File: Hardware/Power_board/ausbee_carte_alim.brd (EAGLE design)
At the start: 64.8 x 71.4 mm, 21 parts

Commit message: modification on power board: add relay and fuse
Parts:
- added D1: 1N4148DO35-10, diode:DO35-10
- added JP1: (no value), pinhead:1X01
- added K1: G5LE, relay:G5LE
- added R4: 10k, rcl:0309V
- added T1: 2N2222, transistor:TO18
- added U$3: FUSE_CAR, eirbot:FUSE_CAR
- moved C3 33.7 mm to (61.6, 64.5)
- moved 12V 32.4 mm to (74.3, 45.7)
- moved 5V 32.4 mm to (74.3, 17.8)
- moved H2 32.4 mm to (90.8, 5.71)
- moved H3 32.4 mm to (90.8, 65.4)
- moved R2 32.4 mm to (74.3, 25.4)
- moved R3 32.4 mm to (74.3, 38.1)
- moved C1 32.4 mm to (61.6, 41.9)
- moved C4 32.4 mm to (61.6, 29.2)
- moved U$1 32.4 mm to (61.6, 55.9)
- moved U$2 32.4 mm to (61.6, 14.0)
- moved 12V_FAN 32.4 mm to (85.7, 50.8)
- moved 12V_MOT 32.4 mm to (85.7, 34.3)
- moved 5V_POW 32.4 mm to (85.7, 19.1)
- moved C2 29.8 mm to (61.6, 6.35)
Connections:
- new net N$4: C1.+, C4.+, K1.P, U$1.3, U$2.3
- new net N$5: D1.A, K1.2, T1.3
- new net N$6: JP1.1, R4.2, T1.2
- new net OUT_FUSE: D1.C, K1.1, K1.O, U$3.P$1
- net GND: now also R4.1, T1.1
- net OUT_ARR_URGENCE: now also U$3.P$2; no longer C1.+, C4.+, U$1.3, U$2.3
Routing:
- net N$4: track 0.00 -> 53.3 mm
- net GND: track 237.9 -> 286.4 mm
- net OUT_ARR_URGENCE: track 65.8 -> 18.4 mm
- net OUT_FUSE: track 0.00 -> 41.8 mm
- net N$5: track 0.00 -> 19.5 mm
- net N$6: track 0.00 -> 10.8 mm
- net N$7: track 0.00 -> 3.18 mm
- net +12V: track 64.2 -> 65.8 mm
- net +5V: track 42.6 -> 43.6 mm
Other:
- board size 64.8 x 71.4 mm -> 97.1 x 71.4 mm
- board text added: "2014"
- board text added: "AUSBEE'done"
- board text added: "CMD_RELAY"

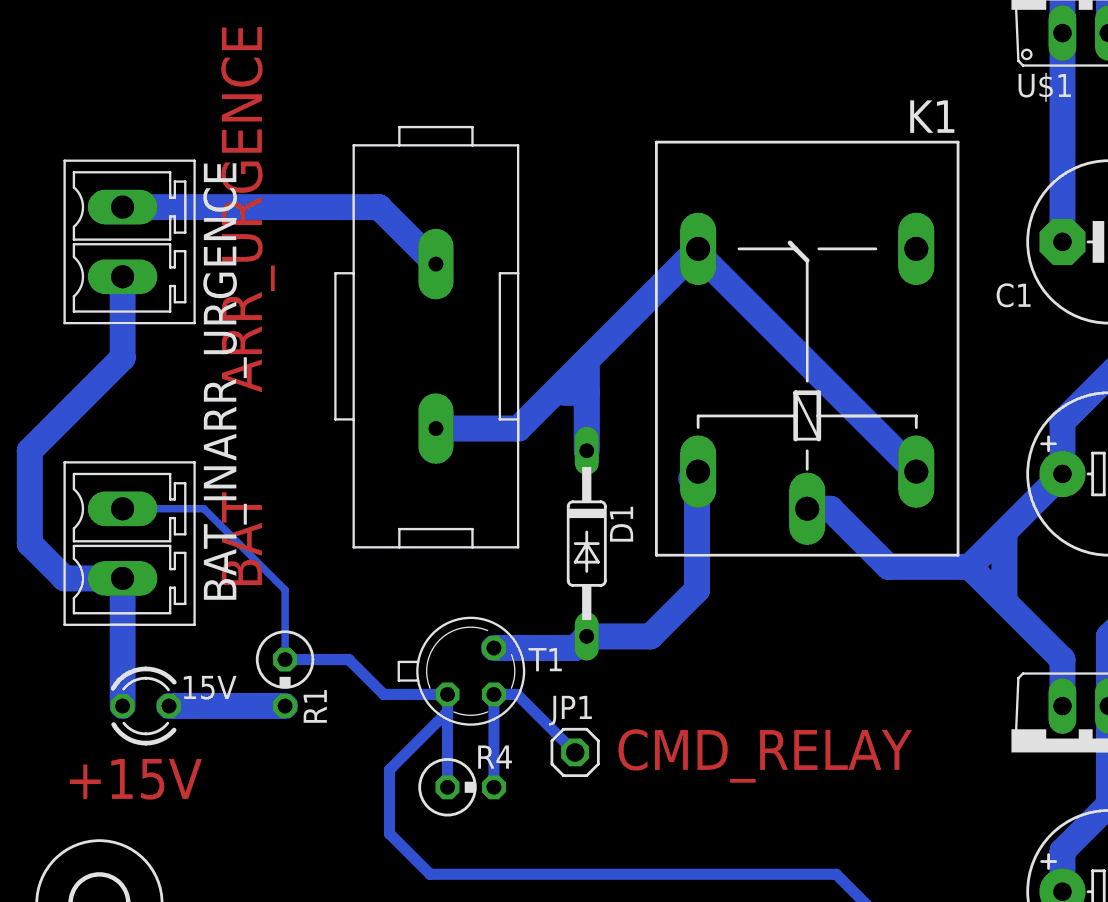
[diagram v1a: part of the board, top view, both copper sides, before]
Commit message: add MOS instead of bipolar and change fuse footprint
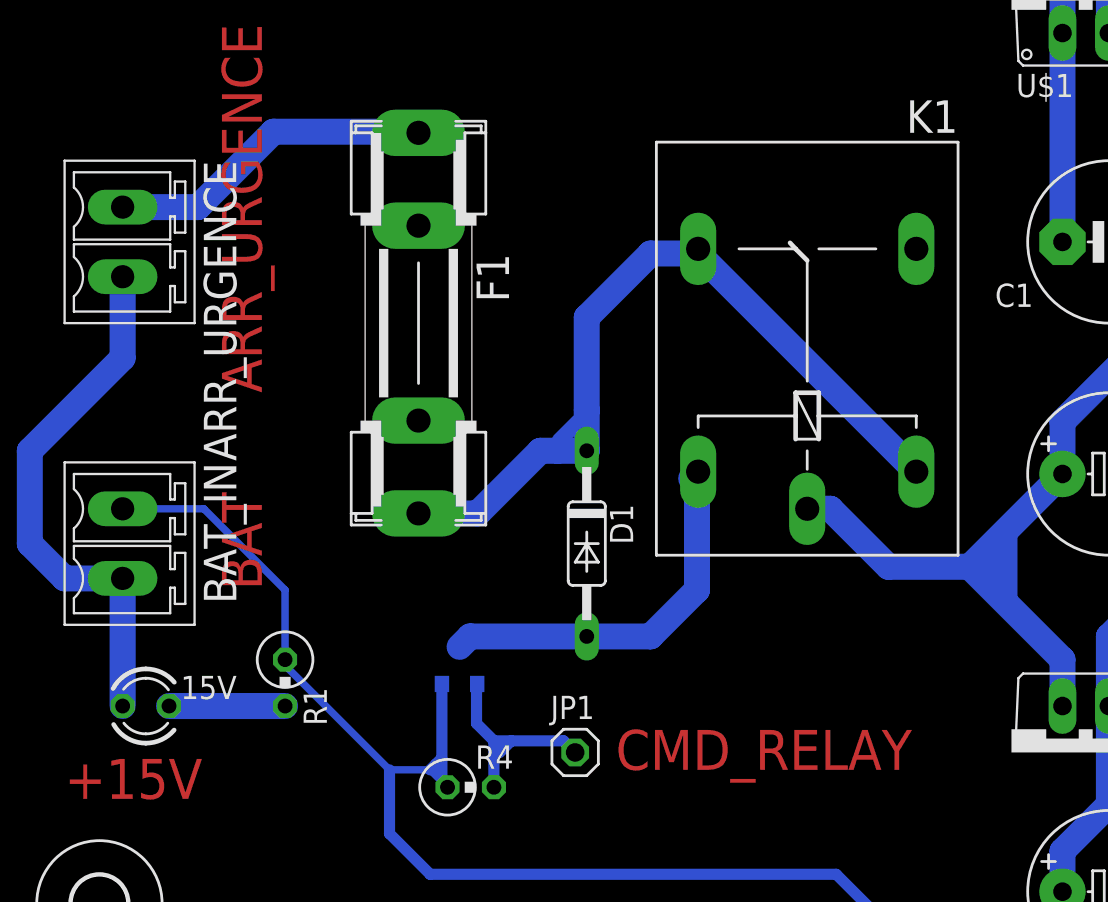
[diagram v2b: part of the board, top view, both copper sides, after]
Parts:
- removed U$3: FUSE_CAR, eirbot:FUSE_CAR
- added F1: FUSESHK20L, fuse:SHK20L
- T1: value 2N2222 -> (none); device transistor:TO18 -> zetex:SOT-23
- moved T1 0.71 mm to (26.0, 18.7), flipped to the bottom, turned to 180 degrees
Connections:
- net GND: now also T1.2; no longer T1.1
- net N$5: now also T1.1; no longer T1.3
- net N$6: now also T1.3; no longer T1.2
- net OUT_ARR_URGENCE: now also F1.1A; no longer U$3.P$2
- net OUT_FUSE: now also F1.2A; no longer U$3.P$1
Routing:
- net OUT_FUSE: track 41.8 -> 47.7 mm
- net N$5: track 19.5 -> 21.3 mm
- net GND: track 286.4 -> 284.8 mm
- net N$8: track 0.00 -> 1.27 mm
- net N$6: track 10.8 -> 11.7 mm
- net OUT_ARR_URGENCE: track 18.4 -> 17.9 mm
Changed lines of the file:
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@@
 <attribute name="OC_FARNELL" value="unknown" x="45.085" y="36.83" size="1.778" layer="27" rot="R90" display="off"/>
 </element>
-<element name="T1" library="transistor" package="TO18" value="2N2222" x="26.67" y="18.415"/>
 <element name="R4" library="rcl" package="0309V" value="10k" x="26.67" y="12.065"/>
 <element name="JP1" library="pinhead" package="1X01" value="" x="32.385" y="13.97"/>
-<element name="U$3" library="eirbot" package="FUSE_CAR" value="FUSE_CAR" x="24.765" y="36.195"/>
 <element name="D1" library="diode" package="DO35-10" value="1N4148DO35-10" x="33.02" y="25.4" rot="R270"/>
+<element name="T1" library="zetex" package="SOT-23" value="" x="26.035" y="18.7325" rot="MR180">
+<attribute name="OC_NEWARK" value="unknown" x="26.035" y="18.7325" size="1.778" layer="28" rot="MR180" display="off"/>
+<attribute name="MPN" value="" x="26.035" y="18.7325" size="1.778" layer="28" rot="MR180" display="off"/>
+<attribute name="MF" value="" x="26.035" y="18.7325" size="1.778" layer="28" rot="MR180" display="off"/>
+<attribute name="OC_FARNELL" value="unknown" x="26.035" y="18.7325" size="1.778" layer="28" rot="MR180" display="off"/>
+</element>
+<element name="F1" library="fuse" package="SHK20L" value="FUSESHK20L" x="23.8125" y="37.465" rot="R270">
+<attribute name="OC_NEWARK" value="unknown" x="23.8125" y="37.465" size="1.778" layer="27" rot="R270" display="off"/>
+<attribute name="MPN" value="" x="23.8125" y="37.465" size="1.778" layer="27" rot="R270" display="off"/>
+<attribute name="MF" value="" x="23.8125" y="37.465" size="1.778" layer="27" rot="R270" display="off"/>
+<attribute name="OC_FARNELL" value="unknown" x="23.8125" y="37.465" size="1.778" layer="27" rot="R270" display="off"/>
+</element>
 </elements>
 <signals>
@@
 <wire x1="61.9125" y1="69.5325" x2="59.055" y2="64.4525" width="0.6096" layer="16"/>
 <wire x1="85.725" y1="46.355" x2="85.725" y2="48.895" width="0.6096" layer="16"/>
-<contactref element="T1" pad="1"/>
 <contactref element="R4" pad="1"/>
-<wire x1="25.4" y1="17.145" x2="25.4" y2="12.065" width="0.6096" layer="16"/>
-<wire x1="25.4" y1="17.145" x2="21.9075" y2="17.145" width="0.6096" layer="16"/>
-<wire x1="21.9075" y1="17.145" x2="20.0025" y2="19.05" width="0.6096" layer="16"/>
-<wire x1="20.0025" y1="19.05" x2="16.51" y2="19.05" width="0.6096" layer="16"/>
-<wire x1="25.4" y1="17.145" x2="25.4" y2="16.1925" width="0.6096" layer="16"/>
-<wire x1="25.4" y1="16.1925" x2="22.225" y2="13.0175" width="0.6096" layer="16"/>
 <wire x1="22.225" y1="13.0175" x2="22.225" y2="9.525" width="0.6096" layer="16"/>
 <wire x1="22.225" y1="9.525" x2="24.4475" y2="7.3025" width="0.6096" layer="16"/>
@@
 <wire x1="64.135" y1="6.35" x2="64.135" y2="16.51" width="1.4224" layer="16"/>
 <wire x1="59.055" y1="53.34" x2="59.055" y2="64.4525" width="1.4224" layer="16"/>
+<contactref element="T1" pad="2"/>
+<wire x1="25.0952" y1="17.7165" x2="25.0952" y2="12.3698" width="0.6096" layer="16"/>
+<wire x1="25.0952" y1="12.3698" x2="25.4" y2="12.065" width="0.4064" layer="16"/>
+<wire x1="16.51" y1="19.05" x2="16.51" y2="18.7325" width="0.4064" layer="16"/>
+<wire x1="16.51" y1="18.7325" x2="22.225" y2="13.0175" width="0.4064" layer="16"/>
+<wire x1="22.225" y1="13.0175" x2="24.4475" y2="13.0175" width="0.4064" layer="16"/>
+<wire x1="24.4475" y1="13.0175" x2="25.4" y2="12.065" width="0.4064" layer="16"/>
+<wire x1="24.4475" y1="13.0175" x2="24.765" y2="13.335" width="0.6096" layer="16"/>
+<wire x1="24.765" y1="13.335" x2="25.0825" y2="13.6525" width="0.6096" layer="16"/>
 </signal>
 <signal name="+5V">
@@
 <signal name="OUT_ARR_URGENCE">
 <contactref element="ARR_URGENCE" pad="1"/>
-<contactref element="U$3" pad="P$2"/>
-<wire x1="7.62" y1="43.815" x2="21.645" y2="43.815" width="1.4224" layer="16"/>
-<wire x1="21.645" y1="43.815" x2="24.765" y2="40.695" width="1.4224" layer="16"/>
+<contactref element="F1" pad="1A"/>
+<wire x1="7.62" y1="43.815" x2="11.7475" y2="43.815" width="1.4224" layer="16"/>
+<wire x1="11.7475" y1="43.815" x2="15.875" y2="47.9425" width="1.4224" layer="16"/>
+<wire x1="15.875" y1="47.9425" x2="23.749" y2="47.9425" width="1.4224" layer="16"/>
+<wire x1="23.749" y1="47.9425" x2="23.8125" y2="47.879" width="1.4224" layer="16"/>
 </signal>
 <signal name="N$1">
@@
 </signal>
 <signal name="N$5">
-<contactref element="T1" pad="3"/>
 <contactref element="K1" pad="2"/>
 <contactref element="D1" pad="A"/>
@@
 <wire x1="39.0525" y1="22.86" x2="39.0525" y2="29.2735" width="1.4224" layer="16"/>
 <wire x1="39.0525" y1="29.2735" x2="39.116" y2="29.337" width="1.4224" layer="16"/>
-<wire x1="27.94" y1="19.685" x2="32.385" y2="19.685" width="1.4224" layer="16"/>
-<wire x1="32.385" y1="19.685" x2="33.02" y2="20.32" width="1.4224" layer="16"/>
+<contactref element="T1" pad="1"/>
+<wire x1="26.0604" y1="19.7485" x2="26.6319" y2="20.32" width="1.4224" layer="16"/>
+<wire x1="26.6319" y1="20.32" x2="33.02" y2="20.32" width="1.4224" layer="16"/>
 </signal>
 <signal name="N$6">
 <contactref element="R4" pad="2"/>
-<contactref element="T1" pad="2"/>
 <contactref element="JP1" pad="1"/>
-<wire x1="27.94" y1="12.065" x2="27.94" y2="17.145" width="0.6096" layer="16"/>
-<wire x1="27.94" y1="17.145" x2="29.21" y2="17.145" width="0.6096" layer="16"/>
-<wire x1="29.21" y1="17.145" x2="32.385" y2="13.97" width="0.6096" layer="16"/>
+<contactref element="T1" pad="3"/>
+<wire x1="27.94" y1="12.065" x2="27.94" y2="14.605" width="0.6096" layer="16"/>
+<wire x1="27.94" y1="14.605" x2="26.9875" y2="15.5575" width="0.6096" layer="16"/>
+<wire x1="26.9875" y1="15.5575" x2="26.9875" y2="17.6784" width="0.6096" layer="16"/>
+<wire x1="26.9875" y1="17.6784" x2="27.0256" y2="17.7165" width="0.4064" layer="16"/>
+<wire x1="32.385" y1="13.97" x2="31.75" y2="14.605" width="0.6096" layer="16"/>
+<wire x1="31.75" y1="14.605" x2="28.8925" y2="14.605" width="0.6096" layer="16"/>
+<wire x1="28.8925" y1="14.605" x2="27.94" y2="14.605" width="0.6096" layer="16"/>
+<wire x1="28.2575" y1="13.97" x2="28.8925" y2="14.605" width="0.6096" layer="16"/>
 </signal>
 <signal name="OUT_FUSE">
-<contactref element="U$3" pad="P$1"/>
 <contactref element="K1" pad="1"/>
 <contactref element="K1" pad="O"/>
 <contactref element="D1" pad="C"/>
-<wire x1="24.765" y1="31.695" x2="29.282" y2="31.695" width="1.4224" layer="16"/>
-<wire x1="29.282" y1="31.695" x2="33.02" y2="35.433" width="1.4224" layer="16"/>
-<wire x1="33.02" y1="35.433" x2="39.116" y2="41.529" width="1.4224" layer="16"/>
 <wire x1="39.116" y1="41.529" x2="39.116" y2="41.275" width="1.016" layer="16"/>
 <wire x1="39.116" y1="41.275" x2="51.054" y2="29.337" width="1.4224" layer="16"/>
-<wire x1="33.02" y1="30.48" x2="33.02" y2="33.655" width="1.4224" layer="16"/>
-<wire x1="33.02" y1="33.655" x2="33.02" y2="35.433" width="1.4224" layer="16"/>
-<wire x1="31.75" y1="33.655" x2="33.02" y2="33.655" width="1.4224" layer="16"/>
+<contactref element="F1" pad="2A"/>
+<wire x1="23.8125" y1="27.051" x2="27.051" y2="27.051" width="1.4224" layer="16"/>
+<wire x1="27.051" y1="27.051" x2="30.48" y2="30.48" width="1.4224" layer="16"/>
+<wire x1="30.48" y1="30.48" x2="31.4325" y2="30.48" width="1.4224" layer="16"/>
+<wire x1="31.4325" y1="30.48" x2="33.02" y2="30.48" width="1.4224" layer="16"/>
+<wire x1="39.116" y1="41.275" x2="36.5125" y2="41.275" width="1.4224" layer="16"/>
+<wire x1="36.5125" y1="41.275" x2="33.02" y2="37.7825" width="1.4224" layer="16"/>
+<wire x1="33.02" y1="37.7825" x2="33.02" y2="32.7025" width="1.4224" layer="16"/>
+<wire x1="33.02" y1="32.7025" x2="33.02" y2="30.48" width="1.4224" layer="16"/>
+<wire x1="31.4325" y1="31.115" x2="33.02" y2="32.7025" width="0.6096" layer="16"/>
+<wire x1="33.02" y1="32.7025" x2="33.02" y2="32.385" width="0.6096" layer="16"/>
+<wire x1="33.02" y1="32.385" x2="31.75" y2="31.115" width="0.6096" layer="16"/>
+<wire x1="31.75" y1="31.115" x2="31.75" y2="30.7975" width="0.6096" layer="16"/>
+<wire x1="31.75" y1="30.7975" x2="31.4325" y2="30.48" width="0.6096" layer="16"/>
 </signal>
 <signal name="N$7">
 <wire x1="55.88" y1="25.7175" x2="55.88" y2="22.5425" width="1.4224" layer="16"/>
 </signal>
+<signal name="N$8">
+<wire x1="54.9275" y1="24.765" x2="54.9275" y2="23.8125" width="0.6096" layer="16"/>
+<wire x1="54.9275" y1="23.8125" x2="55.245" y2="23.8125" width="0.6096" layer="16"/>
+</signal>
 </signals>

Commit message: Power board V2, adaptator GPIO
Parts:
- C2, C3: device rcl:E5-8,5 -> rcl:CT7343
- moved C3 8.09 mm to (53.7, 62.9), flipped to the bottom, turned to 0 degrees
- moved C2 7.47 mm to (68.9, 7.94), flipped to the bottom, turned to 180 degrees
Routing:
- net GND: track 284.8 -> 253.4 mm
- net +12V: track 65.8 -> 71.2 mm
- net N$9: track 0.00 -> 2.86 mm
- net +5V: track 43.6 -> 44.2 mm
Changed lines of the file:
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@@
 <element name="U$2" library="perso_lib" package="TO220V" value="LT1084CT-5" x="61.595" y="13.97" rot="R180"/>
 <element name="C1" library="rcl" package="E5-8,5" value="10u" x="61.595" y="41.91" rot="R180"/>
-<element name="C2" library="rcl" package="E5-8,5" value="22u" x="61.595" y="6.35"/>
-<element name="C3" library="rcl" package="E5-8,5" value="22u" x="61.595" y="64.4525" rot="R180"/>
+<element name="C2" library="rcl" package="CT7343" value="22u" x="68.8975" y="7.9375" rot="MR180"/>
+<element name="C3" library="rcl" package="CT7343" value="22u" x="53.6575" y="62.865" rot="MR0"/>
 <element name="C4" library="rcl" package="E5-8,5" value="10u" x="61.595" y="29.21"/>
 <element name="ARR_URGENCE" library="con-phoenix-381_l" package="MCV2" value="MCV2" x="7.62" y="41.91" rot="R270"/>
@@
 <wire x1="89.535" y1="48.895" x2="92.71" y2="52.07" width="0.6096" layer="16"/>
 <wire x1="92.71" y1="52.07" x2="92.71" y2="53.975" width="0.6096" layer="16"/>
-<wire x1="92.71" y1="53.975" x2="86.36" y2="60.325" width="0.6096" layer="16"/>
-<wire x1="86.36" y1="60.325" x2="72.39" y2="60.325" width="0.6096" layer="16"/>
-<wire x1="72.39" y1="60.325" x2="65.7225" y2="69.5325" width="0.6096" layer="16"/>
-<wire x1="65.7225" y1="69.5325" x2="61.9125" y2="69.5325" width="0.6096" layer="16"/>
-<wire x1="61.9125" y1="69.5325" x2="59.055" y2="64.4525" width="0.6096" layer="16"/>
+<wire x1="92.71" y1="53.975" x2="86.83625" y2="59.84875" width="0.6096" layer="16"/>
+<wire x1="86.83625" y1="59.84875" x2="86.36" y2="60.325" width="0.6096" layer="16"/>
 <wire x1="85.725" y1="46.355" x2="85.725" y2="48.895" width="0.6096" layer="16"/>
 <contactref element="R4" pad="1"/>
@@
 <wire x1="24.4475" y1="7.3025" x2="46.6725" y2="7.3025" width="0.6096" layer="16"/>
 <wire x1="46.6725" y1="7.3025" x2="50.8" y2="3.175" width="0.6096" layer="16"/>
-<wire x1="50.8" y1="3.175" x2="64.77" y2="3.175" width="0.6096" layer="16"/>
 <polygon width="1.4224" layer="16" isolate="1.016">
 <vertex x="-2.54" y="73.025"/>
@@
 <vertex x="-2.54" y="-3.175"/>
 </polygon>
-<wire x1="64.77" y1="3.175" x2="65.405" y2="3.175" width="0.6096" layer="16"/>
-<wire x1="64.135" y1="6.35" x2="80.645" y2="6.35" width="1.4224" layer="16"/>
 <wire x1="80.645" y1="6.35" x2="85.725" y2="11.43" width="1.4224" layer="16"/>
 <wire x1="85.725" y1="11.43" x2="85.725" y2="17.145" width="1.4224" layer="16"/>
-<wire x1="64.135" y1="6.35" x2="64.135" y2="5.3975" width="1.4224" layer="16"/>
-<wire x1="64.135" y1="5.3975" x2="65.7225" y2="3.81" width="1.4224" layer="16"/>
-<wire x1="65.7225" y1="3.81" x2="65.405" y2="3.81" width="1.4224" layer="16"/>
-<wire x1="65.405" y1="3.81" x2="64.77" y2="3.175" width="1.4224" layer="16"/>
-<wire x1="64.135" y1="6.35" x2="64.135" y2="16.51" width="1.4224" layer="16"/>
-<wire x1="59.055" y1="53.34" x2="59.055" y2="64.4525" width="1.4224" layer="16"/>
 <contactref element="T1" pad="2"/>
 <wire x1="25.0952" y1="17.7165" x2="25.0952" y2="12.3698" width="0.6096" layer="16"/>
@@
 <wire x1="22.225" y1="13.0175" x2="24.4475" y2="13.0175" width="0.4064" layer="16"/>
 <wire x1="24.4475" y1="13.0175" x2="25.4" y2="12.065" width="0.4064" layer="16"/>
-<wire x1="24.4475" y1="13.0175" x2="24.765" y2="13.335" width="0.6096" layer="16"/>
-<wire x1="24.765" y1="13.335" x2="25.0825" y2="13.6525" width="0.6096" layer="16"/>
+<wire x1="24.4475" y1="13.0175" x2="25.0825" y2="13.6525" width="0.6096" layer="16"/>
+<wire x1="65.7225" y1="69.5325" x2="77.1525" y2="69.5325" width="1.4224" layer="16"/>
+<wire x1="77.1525" y1="69.5325" x2="86.83625" y2="59.84875" width="1.4224" layer="16"/>
+<wire x1="77.7875" y1="9.2075" x2="80.645" y2="6.35" width="1.4224" layer="16"/>
+<wire x1="50.8" y1="3.175" x2="77.47" y2="3.175" width="1.4224" layer="16"/>
+<wire x1="77.47" y1="3.175" x2="80.645" y2="6.35" width="1.4224" layer="16"/>
 </signal>
 <signal name="+5V">
@@
 <wire x1="79.375" y1="16.51" x2="83.82" y2="20.955" width="1.4224" layer="16"/>
 <wire x1="83.82" y1="20.955" x2="85.725" y2="20.955" width="1.27" layer="16"/>
-<wire x1="59.055" y1="6.35" x2="59.055" y2="8.5725" width="1.4224" layer="16"/>
-<wire x1="59.055" y1="8.5725" x2="61.595" y2="11.1125" width="1.4224" layer="16"/>
-<wire x1="61.595" y1="11.1125" x2="61.595" y2="16.51" width="1.4224" layer="16"/>
+<wire x1="61.595" y1="16.51" x2="61.595" y2="9.525" width="1.4224" layer="16"/>
+<wire x1="61.595" y1="9.525" x2="63.1825" y2="7.9375" width="1.4224" layer="16"/>
+<wire x1="63.1825" y1="7.9375" x2="65.6975" y2="7.9375" width="1.4224" layer="16"/>
 </signal>
 <signal name="+12V">
@@
 <contactref element="12V_MOT" pad="2"/>
 <contactref element="12V_FAN" pad="2"/>
-<wire x1="85.725" y1="52.705" x2="80.01" y2="52.705" width="1.4224" layer="16"/>
+<wire x1="85.725" y1="52.705" x2="80.3275" y2="52.705" width="1.4224" layer="16"/>
+<wire x1="80.3275" y1="52.705" x2="80.01" y2="52.705" width="1.4224" layer="16"/>
 <wire x1="80.01" y1="52.705" x2="74.295" y2="46.99" width="1.4224" layer="16"/>
-<wire x1="74.295" y1="46.99" x2="74.295" y2="52.07" width="1.4224" layer="16"/>
-<wire x1="74.295" y1="52.07" x2="64.135" y2="64.4525" width="1.4224" layer="16"/>
 <wire x1="74.295" y1="46.99" x2="79.375" y2="46.99" width="1.4224" layer="16"/>
 <wire x1="79.375" y1="46.99" x2="85.725" y2="40.64" width="1.4224" layer="16"/>
 <wire x1="85.725" y1="40.64" x2="85.725" y2="36.195" width="1.4224" layer="16"/>
-<wire x1="61.595" y1="53.34" x2="61.595" y2="57.4675" width="1.4224" layer="16"/>
-<wire x1="61.595" y1="57.4675" x2="64.4525" y2="60.325" width="1.4224" layer="16"/>
-<wire x1="64.4525" y1="60.325" x2="64.4525" y2="64.135" width="1.4224" layer="16"/>
-<wire x1="64.4525" y1="64.135" x2="64.135" y2="64.4525" width="1.4224" layer="16"/>
+<wire x1="74.6125" y1="58.42" x2="80.3275" y2="52.705" width="1.4224" layer="16"/>
+<wire x1="56.8575" y1="62.865" x2="60.0075" y2="62.865" width="1.4224" layer="16"/>
+<wire x1="60.0075" y1="62.865" x2="61.595" y2="61.2775" width="1.4224" layer="16"/>
+<wire x1="61.595" y1="61.2775" x2="61.595" y2="60.325" width="1.4224" layer="16"/>
+<wire x1="61.595" y1="60.325" x2="61.595" y2="58.1025" width="1.4224" layer="16"/>
+<wire x1="61.595" y1="58.1025" x2="61.595" y2="53.34" width="1.4224" layer="16"/>
+<wire x1="74.6125" y1="58.42" x2="61.9125" y2="58.42" width="1.4224" layer="16"/>
+<wire x1="61.9125" y1="58.42" x2="61.595" y2="58.1025" width="1.4224" layer="16"/>
+<wire x1="61.595" y1="60.325" x2="63.1825" y2="58.7375" width="1.4224" layer="16"/>
+<wire x1="63.1825" y1="58.7375" x2="63.1825" y2="58.42" width="1.4224" layer="16"/>
+<wire x1="63.1825" y1="58.42" x2="61.9125" y2="57.15" width="1.4224" layer="16"/>
 </signal>
 <signal name="OUT_ARR_URGENCE">
@@
 <wire x1="54.9275" y1="23.8125" x2="55.245" y2="23.8125" width="0.6096" layer="16"/>
 </signal>
+<signal name="N$9">
+<wire x1="78.4225" y1="54.2925" x2="78.4225" y2="51.435" width="1.4224" layer="16"/>
+</signal>
 </signals>
